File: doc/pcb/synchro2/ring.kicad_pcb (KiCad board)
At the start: 2 copper layers, 45 x 45 mm, 0 parts

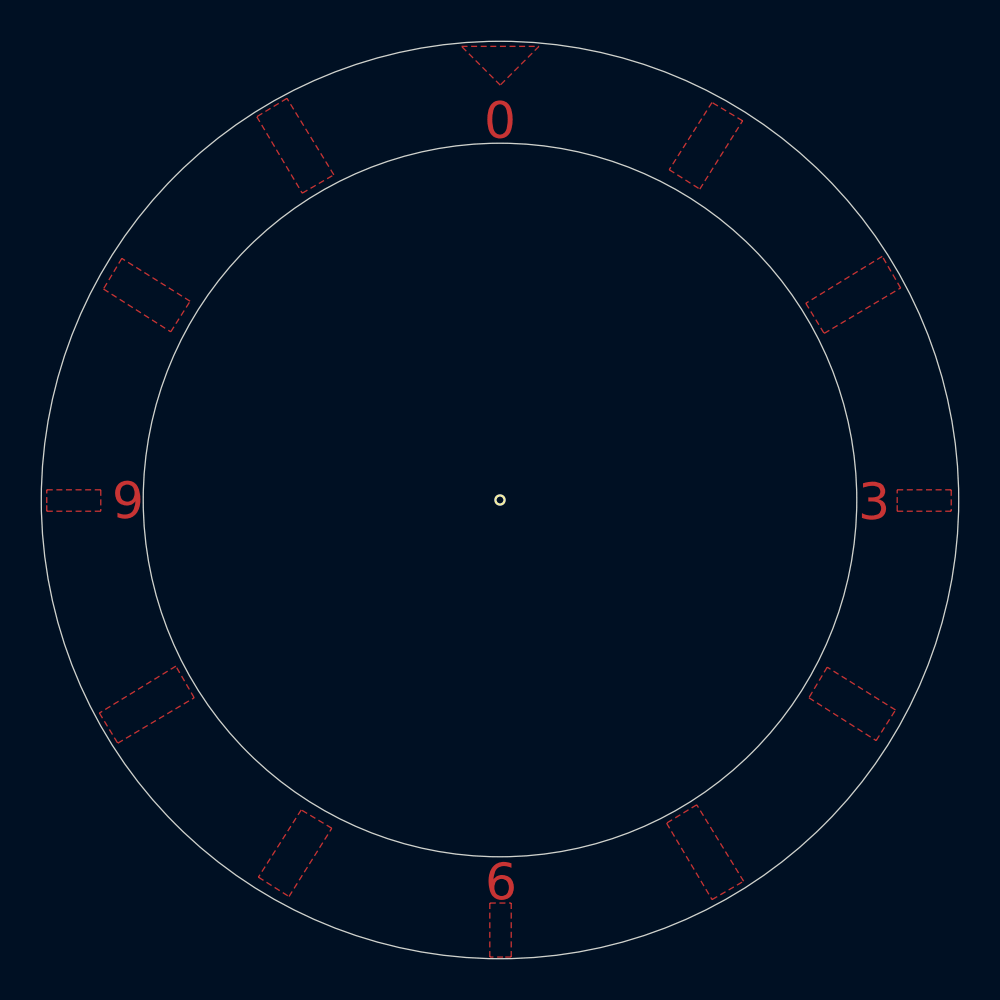
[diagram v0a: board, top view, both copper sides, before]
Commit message: added new version of matrixDisplay, better RING(PCB)
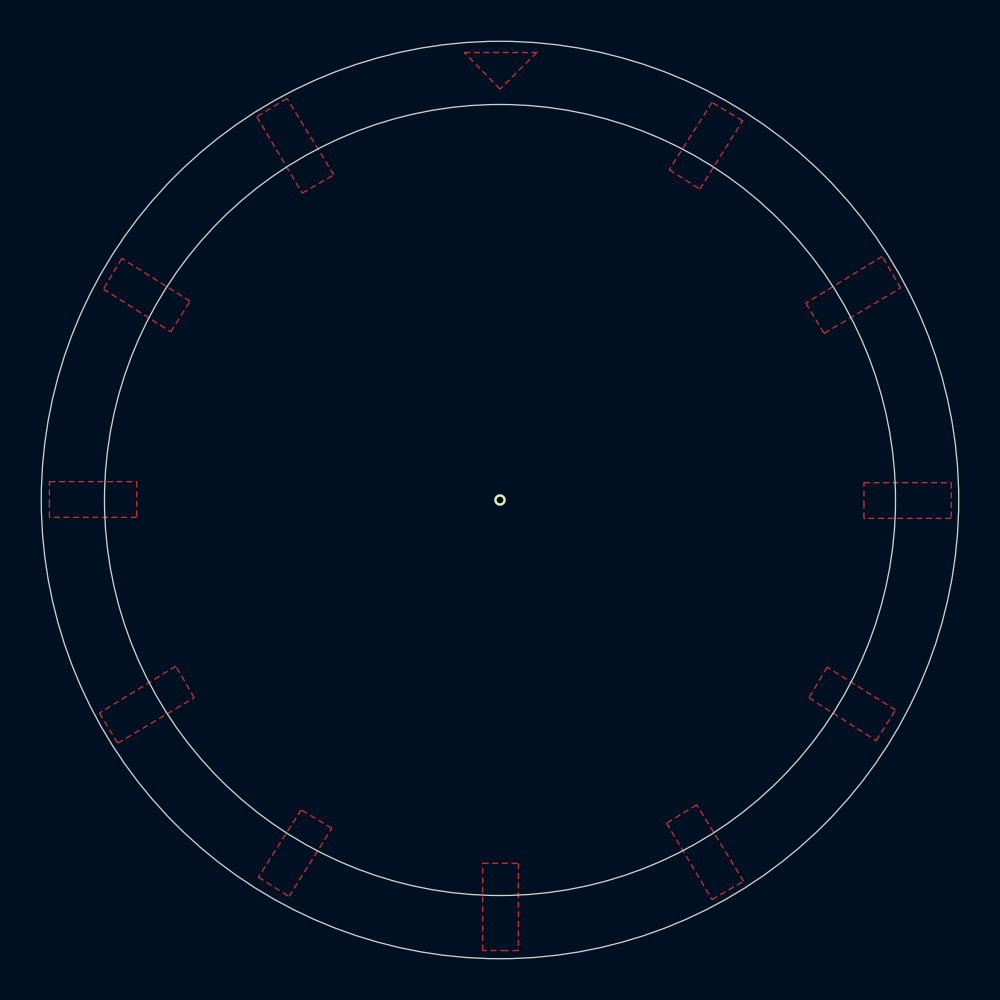
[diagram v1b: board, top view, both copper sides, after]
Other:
- outline, holes or cut-outs redrawn
- board text removed: "0"
- board text removed: "3"
- board text removed: "6"
- board text removed: "9"
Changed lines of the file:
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@@
   (general
     (thickness 1.6)
-    (drawings 20)
+    (drawings 16)
     (tracks 0)
     (zones 0)
@@
   )
   (setup
-    (last_trace_width 0.5)
+    (last_trace_width 0.25)
     (user_trace_width 0.5)
     (trace_clearance 0.2)
@@
     (arrow2b (pts (xy 237.088627 110.562232) (xy 236.440761 111.654555)))
   )
-  (gr_text 9 (at 211.85 99.95) (layer F.Cu)
-    (effects (font (size 1.8 1.8) (thickness 0.3)))
-  )
-  (gr_text 6 (at 230.15 118.65) (layer F.Cu)
-    (effects (font (size 1.8 1.8) (thickness 0.3)))
-  )
-  (gr_text 3 (at 248.45 100) (layer F.Cu)
-    (effects (font (size 1.8 1.8) (thickness 0.3)))
-  )
-  (gr_text 0 (at 230.1 81.3) (layer F.Cu)
-    (effects (font (size 1.8 1.8) (thickness 0.3)))
-  )
   (gr_arc (start 230.1 99.9) (end 218.850001 119.399999) (angle -60) (layer Cmts.User) (width 0.12))
   (gr_arc (start 230.1 99.9) (end 210.600001 88.650001) (angle -60) (layer Cmts.User) (width 0.12))
@@
   (gr_line (start 230.1 99.9) (end 230.1 76.6) (layer Cmts.User) (width 0.12))
   (gr_circle (center 230.1 99.9) (end 230.3 99.8) (layer F.SilkS) (width 0.12))
-  (gr_circle (center 230.1 99.9) (end 247.6 99.9) (layer Edge.Cuts) (width 0.05))
+  (gr_circle (center 230.1 99.9) (end 249.5 99.9) (layer Edge.Cuts) (width 0.05))
   (gr_circle (center 230.1 99.9) (end 252.6 99.9) (layer Edge.Cuts) (width 0.05))
   (zone (net 0) (net_name "") (layer F.Cu) (hatch edge 0.508)
@@
     (polygon
       (pts
-        (xy 230.112118 79.55) (xy 228.212118 77.65) (xy 232.012118 77.65)
-      )
-    )
-  )
-  (zone (net 0) (net_name "") (layer F.Cu) (hatch edge 0.508)
-    (connect_pads (clearance 0.508))
-    (min_thickness 0.254)
-    (fill yes (arc_segments 32) (thermal_gap 0.508) (thermal_bridge_width 0.508))
-    (polygon
-      (pts
-        (xy 249.582342 100.05) (xy 249.582342 99.4) (xy 252.232342 99.4) (xy 252.232342 100.45) (xy 249.582342 100.45)
-      )
-    )
-  )
-  (zone (net 0) (net_name "") (layer F.Cu) (hatch edge 0.508)
-    (connect_pads (clearance 0.508))
-    (min_thickness 0.254)
-    (fill yes (arc_segments 32) (thermal_gap 0.508) (thermal_bridge_width 0.508))
-    (polygon
-      (pts
-        (xy 207.867595 100.05) (xy 207.867595 99.4) (xy 210.517595 99.4) (xy 210.517595 100.45) (xy 207.867595 100.45)
-      )
-    )
-  )
-  (zone (net 0) (net_name "") (layer F.Cu) (hatch edge 0.508)
-    (connect_pads (clearance 0.508))
-    (min_thickness 0.254)
-    (fill yes (arc_segments 32) (thermal_gap 0.508) (thermal_bridge_width 0.508))
-    (polygon
-      (pts
-        (xy 230.25 122.317658) (xy 229.6 122.317658) (xy 229.6 119.667658) (xy 230.65 119.667658) (xy 230.65 122.317658)
+        (xy 230.1 79.75) (xy 228.35 77.95) (xy 231.9 77.95)
+      )
+    )
+  )
+  (zone (net 0) (net_name "") (layer F.Cu) (hatch edge 0.508)
+    (connect_pads (clearance 0.508))
+    (min_thickness 0.254)
+    (fill yes (arc_segments 32) (thermal_gap 0.508) (thermal_bridge_width 0.508))
+    (polygon
+      (pts
+        (xy 247.95 100.2) (xy 247.95 99.05) (xy 252.232342 99.05) (xy 252.232342 100.8) (xy 247.95 100.8)
       )
     )
@@
       )
     )
+  )
+  (zone (net 0) (net_name "") (layer F.Cu) (hatch edge 0.508)
+    (connect_pads (clearance 0.508))
+    (min_thickness 0.254)
+    (fill yes (arc_segments 32) (thermal_gap 0.508) (thermal_bridge_width 0.508))
+    (polygon
+      (pts
+        (xy 208 100.15) (xy 208 99) (xy 212.282342 99) (xy 212.282342 100.75) (xy 208 100.75)
+      )
+    )
+  )
+  (zone (net 0) (net_name "") (layer F.Cu) (hatch edge 0.508)
+    (connect_pads (clearance 0.508))
+    (min_thickness 0.254)
+    (fill yes (arc_segments 32) (thermal_gap 0.508) (thermal_bridge_width 0.508))
+    (polygon
+      (pts
+        (xy 230.4 122) (xy 229.25 122) (xy 229.25 117.717658) (xy 231 117.717658) (xy 231 122)
+      )
+    )

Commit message: added connections for ADC
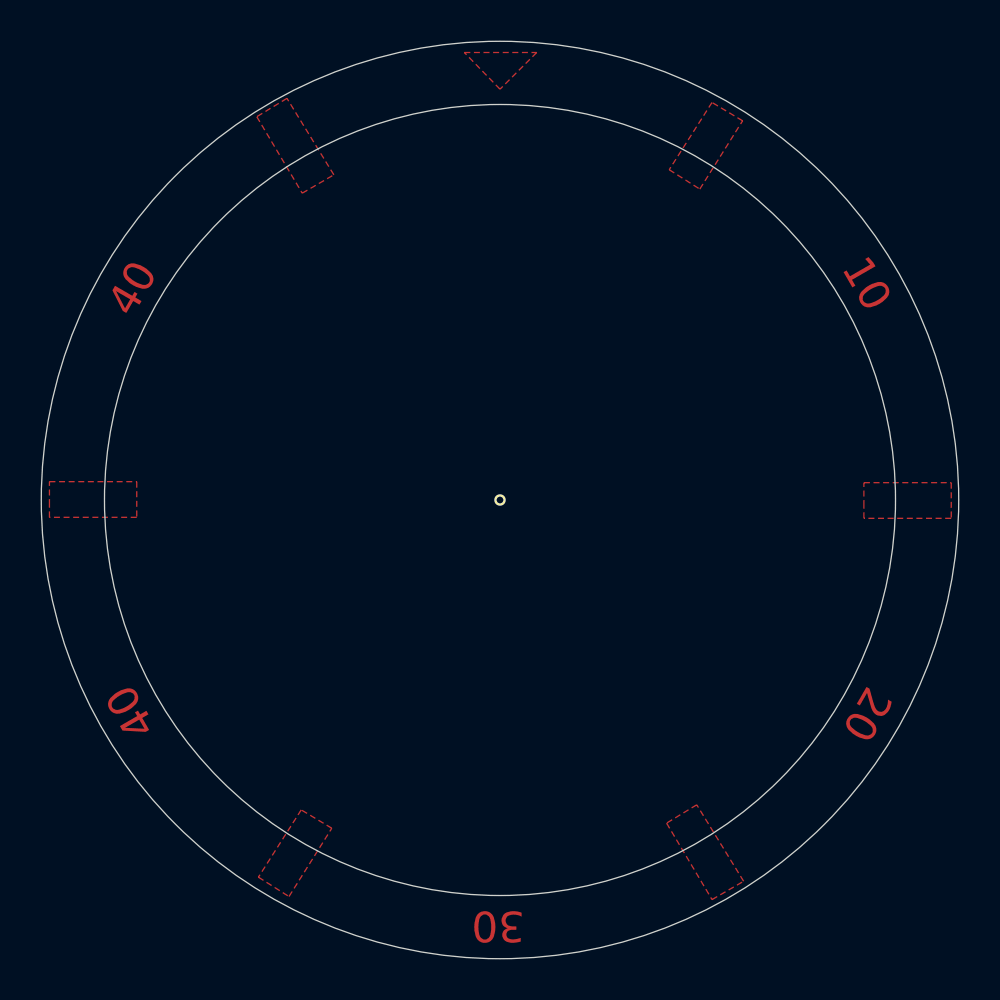
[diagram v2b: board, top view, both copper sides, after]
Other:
- board text added: "10"
- board text added: "20"
- board text added: "30"
- board text added: "40"
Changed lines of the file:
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@@
   (general
     (thickness 1.6)
-    (drawings 16)
+    (drawings 21)
     (tracks 0)
     (zones 0)
@@
     (uvia_drill 0.1)
   )
+  (gr_text 40 (at 212.08 89.51 -300) (layer F.Cu)
+    (effects (font (size 1.5 1.5) (thickness 0.3)))
+  )
+  (gr_text 40 (at 211.99 110.3 -240) (layer F.Cu)
+    (effects (font (size 1.5 1.5) (thickness 0.3)))
+  )
+  (gr_text 30 (at 230.01 120.79 -180) (layer F.Cu)
+    (effects (font (size 1.5 1.5) (thickness 0.3)))
+  )
+  (gr_text 20 (at 248.1 110.42 -120) (layer F.Cu)
+    (effects (font (size 1.5 1.5) (thickness 0.3)))
+  )
+  (gr_text 10 (at 248.08 89.29 -60) (layer F.Cu)
+    (effects (font (size 1.5 1.5) (thickness 0.3)))
+  )
   (dimension 1.706605 (width 0.12) (layer F.SilkS)
     (gr_text "1,707 mm" (at 235.693876 109.933189 31.82744658) (layer F.SilkS)
@@
     (polygon
       (pts
-        (xy 245.1 90.25) (xy 245.999708 91.729395) (xy 249.75 89.5) (xy 248.85 87.95)
-      )
-    )
-  )
-  (zone (net 0) (net_name "") (layer F.Cu) (hatch edge 0.508)
-    (connect_pads (clearance 0.508))
-    (min_thickness 0.254)
-    (fill yes (arc_segments 32) (thermal_gap 0.508) (thermal_bridge_width 0.508))
-    (polygon
-      (pts
-        (xy 210.45 110.35) (xy 211.349708 111.829395) (xy 215.1 109.6) (xy 214.2 108.05)
-      )
-    )
-  )
-  (zone (net 0) (net_name "") (layer F.Cu) (hatch edge 0.508)
-    (connect_pads (clearance 0.508))
-    (min_thickness 0.254)
-    (fill yes (arc_segments 32) (thermal_gap 0.508) (thermal_bridge_width 0.508))
-    (polygon
-      (pts
         (xy 218.25 118.4) (xy 219.75 119.35) (xy 221.85 116) (xy 220.35 115.1)
       )
@@
     (polygon
       (pts
-        (xy 248.55 111.7) (xy 249.5 110.2) (xy 246.15 108.1) (xy 245.25 109.6)
-      )
-    )
-  )
-  (zone (net 0) (net_name "") (layer F.Cu) (hatch edge 0.508)
-    (connect_pads (clearance 0.508))
-    (min_thickness 0.254)
-    (fill yes (arc_segments 32) (thermal_gap 0.508) (thermal_bridge_width 0.508))
-    (polygon
-      (pts
-        (xy 213.95 91.65) (xy 214.9 90.15) (xy 211.55 88.05) (xy 210.65 89.55)
-      )
-    )
-  )
-  (zone (net 0) (net_name "") (layer F.Cu) (hatch edge 0.508)
-    (connect_pads (clearance 0.508))
-    (min_thickness 0.254)
-    (fill yes (arc_segments 32) (thermal_gap 0.508) (thermal_bridge_width 0.508))
-    (polygon
-      (pts
         (xy 208 100.15) (xy 208 99) (xy 212.282342 99) (xy 212.282342 100.75) (xy 208 100.75)
       )
     )
-  )
-  (zone (net 0) (net_name "") (layer F.Cu) (hatch edge 0.508)
-    (connect_pads (clearance 0.508))
-    (min_thickness 0.254)
-    (fill yes (arc_segments 32) (thermal_gap 0.508) (thermal_bridge_width 0.508))
-    (polygon
-      (pts
-        (xy 230.4 122) (xy 229.25 122) (xy 229.25 117.717658) (xy 231 117.717658) (xy 231 122)
-      )
-    )
